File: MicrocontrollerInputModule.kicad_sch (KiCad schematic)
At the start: 46 parts, among them J1 Conn_02x04_Odd_Even, SW1 KXT3, SW2 KXT3, U1 W25Q16JVUXIQ, U2 RP2040, U3 TXB0108DQSR, U4 TXB0108DQSR, Y1 12.000MHz

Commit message: Version 2
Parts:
- removed C19, C20: 0.1uF, Capacitor_SMD:C_0603_1608Metric, symbol Device:C
- removed H1, H2: 24929, InputModule:MountingHole_3.7mm_Pad_24929, symbol Mechanical:MountingHole
- removed H3, H4: MountingHole, MountingHole:MountingHole_2.1mm, symbol Mechanical:MountingHole
- removed J1: Conn_02x04_Odd_Even, InputModule:PogoPads_2x4_P2.0mm, symbol Connector_Generic:Conn_02x04_Odd_Even
- removed R8, R9: 10K, Resistor_SMD:R_0402_1005Metric, symbol Device:R
- removed U3, U4: TXB0108DQSR, FootprintLibrary:USON-20_2x4mm_P0.4mm, symbol Logic_LevelTranslator:TXB0108DQSR
- added F1: Polyfuse 600mA, Resistor_SMD:R_1206_3216Metric, symbol Device:Polyfuse
- added F2: Polyfuse 200mA, Resistor_SMD:R_1206_3216Metric, symbol Device:Polyfuse
- added J2: FH34SRJ-12S-0.5SH_50_, FH34SRJ-12S-0.5SH_50_:HRS_FH34SRJ-12S-0.5SH_50_, symbol FH34SRJ-12S-0.5SH_50_:FH34SRJ-12S-0.5SH_50_
- added R10, R11, R12, R13, R14, R15, R16, R9: 470, Resistor_SMD:R_0402_1005Metric, symbol Device:R_US
- added R24, R8: 10k, Resistor_SMD:R_0402_1005Metric, symbol Device:R_US
- added U3, U4: 74AHC125BQ_115, 74AHC125BQ_115:QFN50P300X250X100-15N, symbol 74AHC125BQ_115:74AHC125BQ_115
- C17, C18: value 0.1uF -> 10uF
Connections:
- net +3V3: now also F2.2; no longer C17.1
- net +5V: now also C17.1, C18.1, F1.1, U3.14 (VCC), U4.14 (VCC); no longer C18.2
- net BOARD_ID: now also J2.4
- net D10: now also U4.5 (2A)
- net D11: now also U4.2 (1A)
- net D12: now also U3.12 (4A)
- net D13: now also U3.9 (3A)
- net D14: now also U3.5 (2A)
- net D15: now also U3.2 (1A)
- net D7: now also R8.2, U3.10 (~{3OE}), U3.13 (~{4OE}), U3.4 (~{2OE}), U4.1 (~{1OE}), U4.10 (~{3OE}), U4.13 (~{4OE}), U4.4 (~{2OE})
- net D8: now also U4.12 (4A)
- net D9: now also U4.9 (3A)
- net GND: now also C18.2, J2.10, J2.5, J2.6, J2.7, J2.S1 (SHIELD), J2.S2 (SHIELD__1), R24.1, R8.1, U3.7 (GND), U4.7 (GND); no longer C18.1
- net NeopixelMatrix/STRIP1: now also R9.2
- net NeopixelMatrix/STRIP11: now also R14.2
- net NeopixelMatrix/STRIP13: now also R15.2
- net NeopixelMatrix/STRIP15: now also R16.2
- net NeopixelMatrix/STRIP3: now also R10.2
- net NeopixelMatrix/STRIP5: now also R11.2
- net NeopixelMatrix/STRIP7: now also R12.2
- net NeopixelMatrix/STRIP9: now also R13.2
- net USB_DN: now also J2.9
- net USB_DP: now also J2.8
- net ~{SLEEP}: now also J2.11
- net D16: no longer names the net of U2.27 (GPIO16)
- net D17: no longer names the net of U2.28 (GPIO17)
- net D21: no longer names the net of U2.32 (GPIO21)
- net D22: no longer names the net of U2.34 (GPIO22)
- net D23: no longer names the net of U2.35 (GPIO23)
- net D5: no longer names the net of U2.7 (GPIO5)
- net D6: no longer names the net of U2.8 (GPIO6)
- net D6: now also R24.2, U3.1 (~{1OE})
- new net: R12.1, U3.11 (4Y)
- new net: R9.1, U3.3 (1Y)
- new net: R16.1, U4.11 (4Y)
- new net: R13.1, U4.3 (1Y)
- new net: R14.1, U4.6 (2Y)
- new net: R15.1, U4.8 (3Y)
- new net: F1.2, J2.1, J2.2, J2.3
- new net: F2.1, J2.12
- new net: R10.1, U3.6 (2Y)
- new net: R11.1, U3.8 (3Y)
- no-connect marks 2 -> 8
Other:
- sheet NeopixelMatrix ports: added none; removed STRIP10, STRIP12, STRIP14, STRIP16, STRIP2, STRIP4, STRIP6, STRIP8
- note added: "By default we want all level shifter outputs to be driven. But, if we want to setup the array as one single LED strip we want to turn off all but the first output."
- note added: "FPC Connector Interface"
- note removed: "1.2-3.6V"
- note removed: "1.65-5.5V"
- note removed: "Spring Connector Interface"
- moved on the sheet: R7

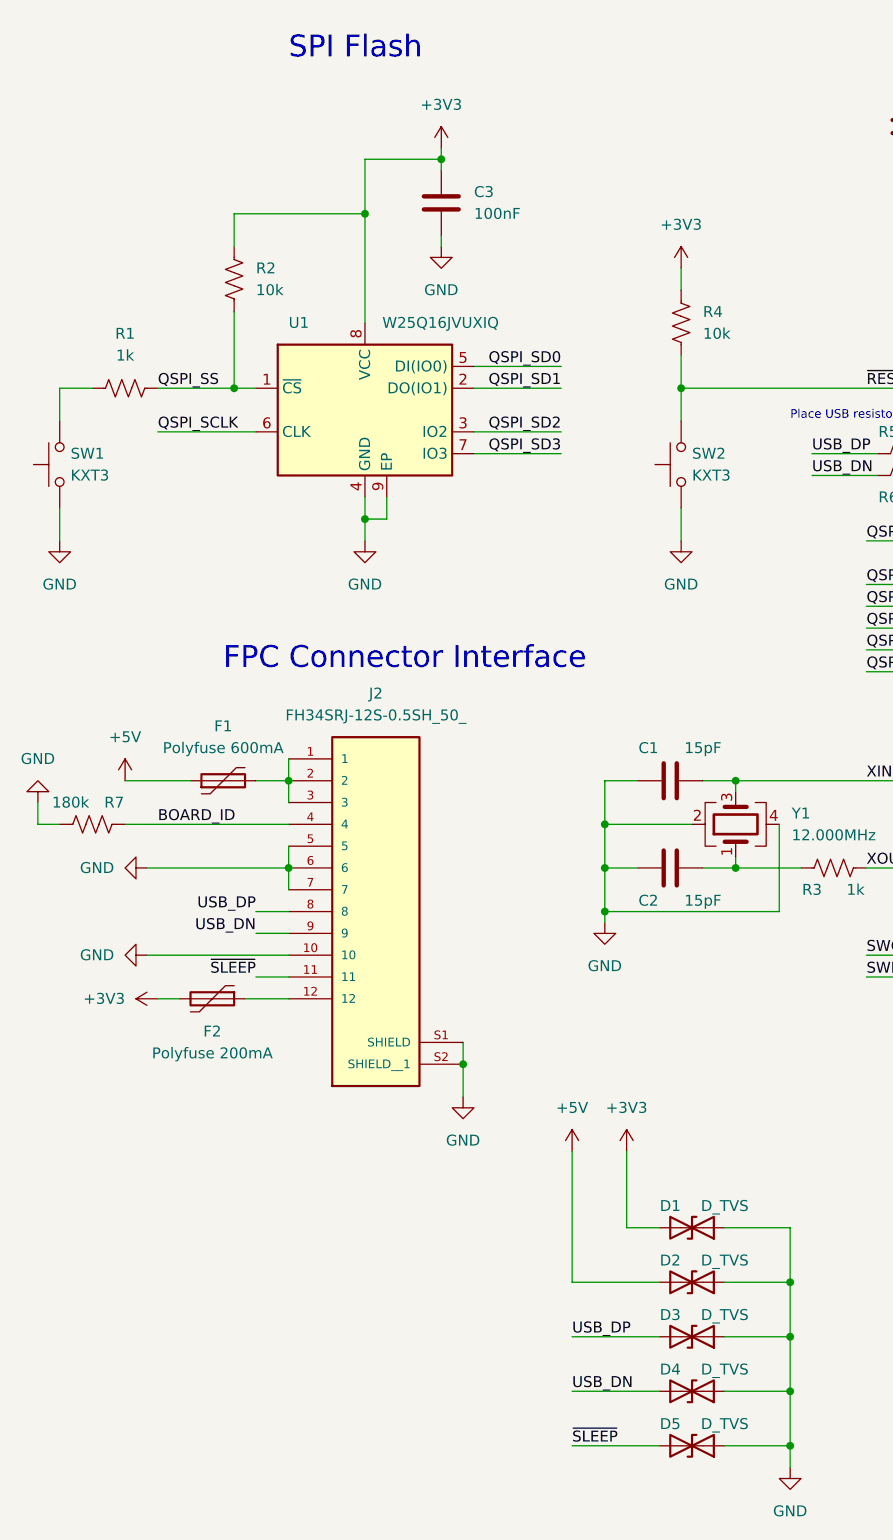
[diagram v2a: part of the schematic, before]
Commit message: Added dip switch
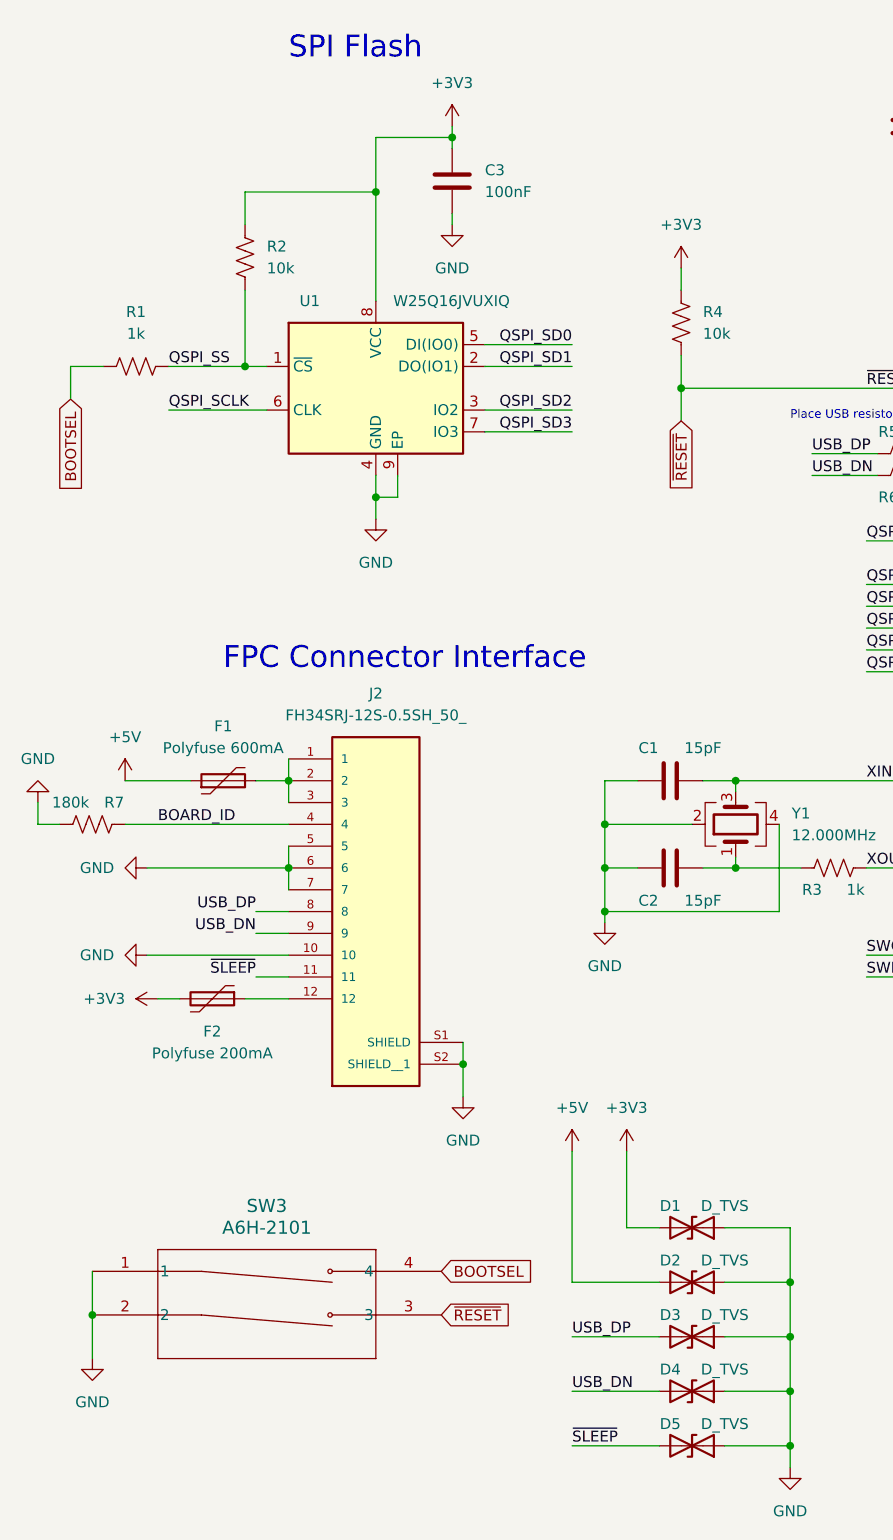
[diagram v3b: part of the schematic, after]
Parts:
- removed SW1, SW2: KXT3, Button_Switch_SMD:SW_SPST_CK_KXT3, symbol Switch:SW_Push
- added SW3: A6H-2101, SW_A6H-2101_OMR, symbol 2023-10-21_03-08-25:A6H-2101
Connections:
- net GND: now also SW3.1, SW3.2
- net ~{RESET}: now also SW3.3
- net BOOTSEL: now reaches R1.1
- net BOOTSEL: now also SW3.4
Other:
- moved on the sheet: C3, R1, R2, U1

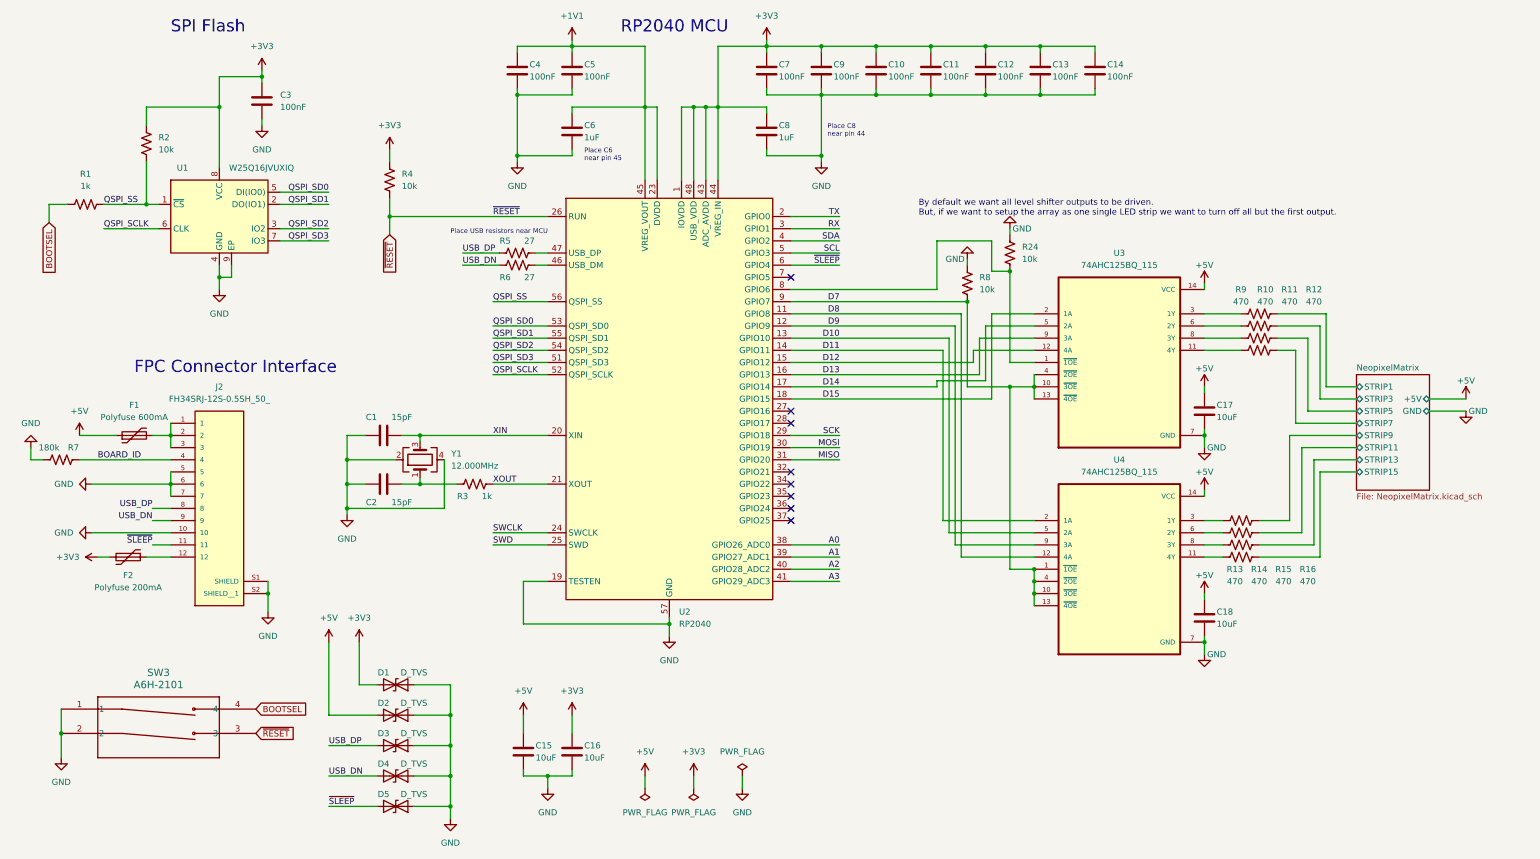
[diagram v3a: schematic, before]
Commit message: Arya Edits and Feedback plus DIP Switch
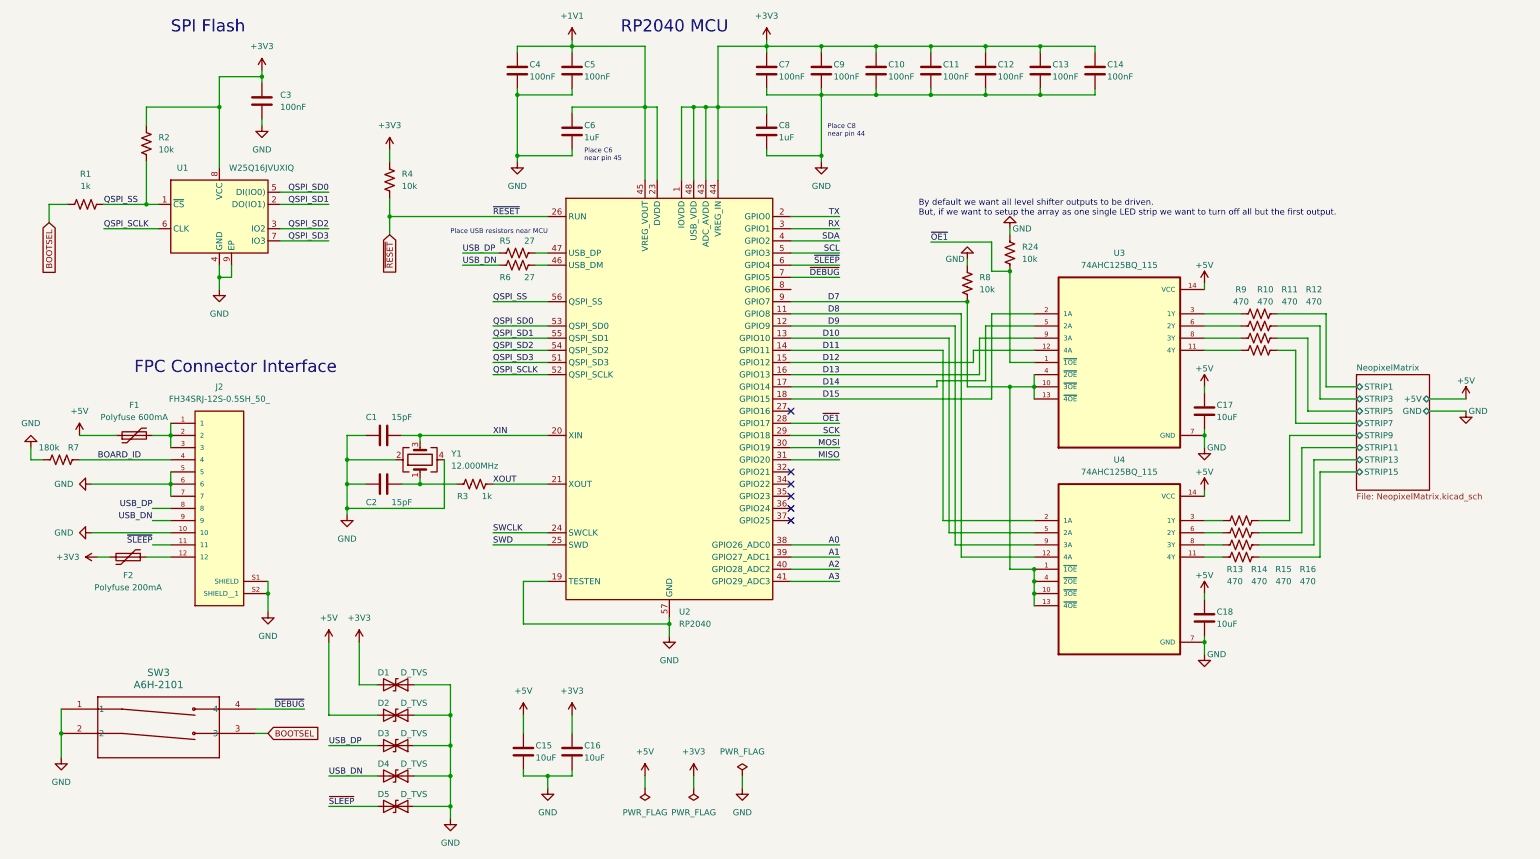
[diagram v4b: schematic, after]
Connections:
- net BOOTSEL: now also SW3.3; no longer SW3.4
- net ~{RESET}: no longer SW3.3
- net ~{OE1}: now reaches U2.28 (GPIO17)
- net ~{OE1}: now also R24.2, U3.1 (~{1OE})
- net ~{DEBUG}: now reaches U2.7 (GPIO5)
- net ~{DEBUG}: now also SW3.4
- now unconnected: U2.8 (GPIO6)
- no-connect marks 8 -> 6
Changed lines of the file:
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@@
   (no_connect (at 177.8 100.33))
   (no_connect (at 177.8 118.11))
-  (no_connect (at 177.8 72.39))
-  (no_connect (at 177.8 102.87))
   (wire (pts (xy 177.8 69.85) (xy 187.96 69.85))
     (stroke (width 0) (type default))
@@
     (stroke (width 0) (type default))
   )
+  (wire (pts (xy 68.58 167.64) (xy 66.04 167.64))
+    (stroke (width 0) (type default))
+  )
   (wire (pts (xy 177.8 59.69) (xy 187.96 59.69))
     (stroke (width 0) (type default))
@@
     (stroke (width 0) (type default))
   )
+  (wire (pts (xy 177.8 72.39) (xy 187.96 72.39))
+    (stroke (width 0) (type default))
+  )
+  (wire (pts (xy 66.04 162.56) (xy 76.2 162.56))
+    (stroke (width 0) (type default))
+  )
   (wire (pts (xy 120.65 46.99) (xy 132.08 46.99))
     (stroke (width 0) (type default))
@@
     (stroke (width 0) (type default))
   )
-  (wire (pts (xy 208.28 74.93) (xy 208.28 64.77))
-    (stroke (width 0) (type default))
-  )
   (wire (pts (xy 177.8 77.47) (xy 214.63 77.47))
     (stroke (width 0) (type default))
@@
     (stroke (width 0) (type default))
   )
+  (wire (pts (xy 187.96 102.87) (xy 177.8 102.87))
+    (stroke (width 0) (type default))
+  )
   (wire (pts (xy 228.6 135.89) (xy 228.6 138.43))
     (stroke (width 0) (type default))
@@
     (stroke (width 0) (type default))
   )
-  (wire (pts (xy 208.28 64.77) (xy 219.71 64.77))
+  (wire (pts (xy 207.01 65.024) (xy 219.71 65.024))
     (stroke (width 0) (type default))
   )
@@
     (stroke (width 0) (type default))
   )
-  (wire (pts (xy 219.71 64.77) (xy 219.71 71.12))
+  (wire (pts (xy 219.71 65.024) (xy 219.71 71.12))
     (stroke (width 0) (type default))
   )
@@
   )
   (wire (pts (xy 311.15 100.33) (xy 318.77 100.33))
-    (stroke (width 0) (type default))
-  )
-  (wire (pts (xy 177.8 74.93) (xy 208.28 74.93))
     (stroke (width 0) (type default))
   )
@@
     (effects (font (size 1.27 1.27)) (justify right bottom))
   )
+  (label "~{DEBUG}" (at 76.2 162.56 180) (fields_autoplaced)
+    (effects (font (size 1.27 1.27)) (justify right bottom))
+  )
   (label "QSPI_SD2" (at 115.57 87.63 0) (fields_autoplaced)
     (effects (font (size 1.27 1.27)) (justify left bottom))
@@
     (effects (font (size 1.27 1.27)) (justify left bottom))
   )
+  (label "~{OE1}" (at 207.01 65.024 0) (fields_autoplaced)
+    (effects (font (size 1.27 1.27)) (justify left bottom))
+  )
   (label "MISO" (at 187.96 110.49 180) (fields_autoplaced)
     (effects (font (size 1.27 1.27)) (justify right bottom))
@@
     (effects (font (size 1.27 1.27)) (justify left bottom))
   )
+  (label "~{OE1}" (at 187.96 102.87 180) (fields_autoplaced)
+    (effects (font (size 1.27 1.27)) (justify right bottom))
+  )
   (label "QSPI_SCLK" (at 115.57 92.71 0) (fields_autoplaced)
     (effects (font (size 1.27 1.27)) (justify left bottom))
@@
     (effects (font (size 1.27 1.27)) (justify right bottom))
   )
+  (label "~{DEBUG}" (at 187.96 72.39 180) (fields_autoplaced)
+    (effects (font (size 1.27 1.27)) (justify right bottom))
+  )
   (label "QSPI_SCLK" (at 34.29 62.23 0) (fields_autoplaced)
     (effects (font (size 1.27 1.27)) (justify left bottom))
@@
     (effects (font (size 1.27 1.27)) (justify left bottom))
   )
-  (global_label "BOOTSEL" (shape input) (at 66.04 162.56 0) (fields_autoplaced)
+  (global_label "BOOTSEL" (shape input) (at 68.58 167.64 0) (fields_autoplaced)
     (effects (font (size 1.27 1.27)) (justify left))
-    (property "Intersheetrefs" "${INTERSHEET_REFS}" (at 77.3104 162.56 0)
+    (property "Intersheetrefs" "${INTERSHEET_REFS}" (at 79.8504 167.64 0)
       (effects (font (size 1.27 1.27)) (justify left) hide)
     )
@@
     )
   )
-  (global_label "~{RESET}" (shape input) (at 66.04 167.64 0) (fields_autoplaced)
-    (effects (font (size 1.27 1.27)) (justify left))
-    (property "Intersheetrefs" "${INTERSHEET_REFS}" (at 74.7703 167.64 0)
-      (effects (font (size 1.27 1.27)) (justify left) hide)
-    )
-  )

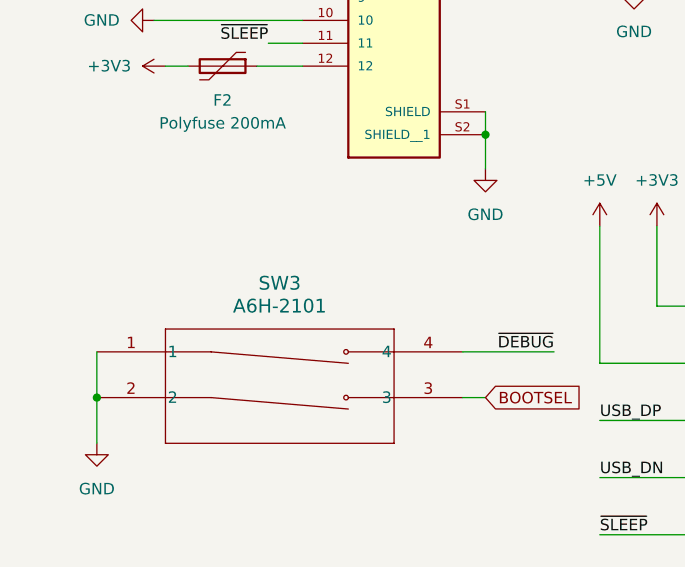
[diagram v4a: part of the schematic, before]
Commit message: Adjusting silk screen and some wires
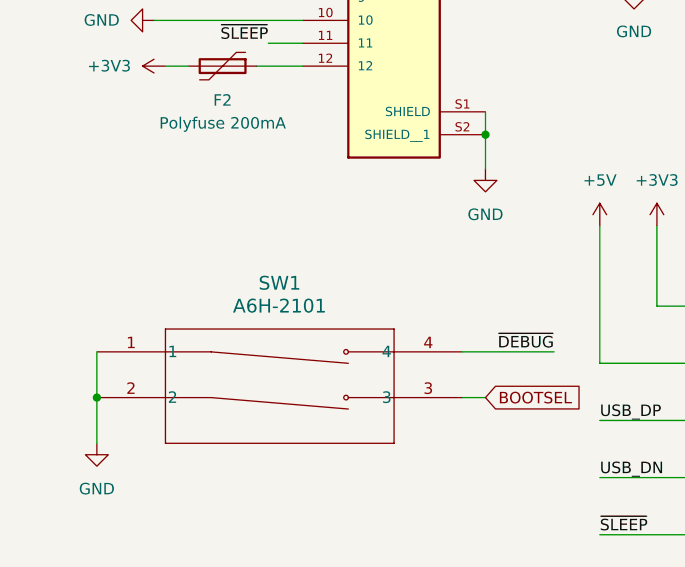
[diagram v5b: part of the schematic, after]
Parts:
- renumbered SW3 to SW1
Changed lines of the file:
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@@
   (symbol (lib_id "2023-10-21_03-08-25:A6H-2101") (at 25.4 162.56 0) (unit 1)
     (in_bom yes) (on_board yes) (dnp no) (fields_autoplaced)
-    (property "Reference" "SW3" (at 45.72 154.94 0)
+    (property "Reference" "SW1" (at 45.72 154.94 0)
       (effects (font (size 1.524 1.524)))
     )
@@
       (project "MicrocontrollerInputModule"
         (path "/e1225fe3-1add-4bf0-8592-1d94311392e6"
-          (reference "SW3") (unit 1)
+          (reference "SW1") (unit 1)
         )
       )

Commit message: V3 update in preparation for sale
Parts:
- C1, C2: LCSC Part # (none) -> C76950
- C10, C11, C12, C13, C14, C3, C4, C5, C7, C9: LCSC Part # (none) -> C1525
- C15, C16, C17, C18: LCSC Part # (none) -> C19702
- C6, C8: LCSC Part # (none) -> C29266
- D1, D2, D3, D4, D5: LCSC Part # (none) -> C468904
- F1: LCSC Part # (none) -> C883122
- F2: LCSC Part # (none) -> C910826
- J2: LCSC Part # (none) -> C424659
- R1, R3: LCSC Part # (none) -> C106235
- R10, R11, R12, R13, R14, R15, R16, R9: LCSC Part # (none) -> C25117
- R2, R24, R4, R8: LCSC Part # (none) -> C60490
- R5, R6: LCSC Part # (none) -> C138021
- R7: LCSC Part # (none) -> C138046
- SW1: LCSC Part # (none) -> C224990
- U1: LCSC Part # (none) -> C2843335
- U2: LCSC Part # (none) -> C2040
- U3, U4: LCSC Part # (none) -> C554218
- Y1: LCSC Part # (none) -> C7294551
